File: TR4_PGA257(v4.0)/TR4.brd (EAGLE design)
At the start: 204 x 172 mm, 159 parts, among them IC1 SN74AVC4T774PWR, IC2 W25Q256JVFIQ, IC3 SN74AVC4T774PWR, IC4 SN74AVC4T774PWR, IC6 CP2102-GMR, IC7 LM1117MP-1.8_NOPB, IC8 LM1117MP-1.8_NOPB, IC9 LM1117MP-1.8_NOPB, J1 U-F-M5DD-Y-L, J3 TF-15X15, J4 2985-6004, J5 2985-6004, Q1 FMMT497TA, Q10 BSH103,235, Q11 BSH103,235, Q12 BSH103,235, Q13 BSH103,235, Q2 FMMT497TA, Q3 BSH103,235, Q4 BSH103,235, Q5 BSH103,235, Q6 BSH103,235, Q7 BSH103,235, Q8 BSH103,235, Q9 BSH103,235

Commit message: Add pull resistor for mosfet
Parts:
- added R61, R62, R63, R64, R65, R66, R67, R68, R69, R70, R71: 10k, SparkFun-Resistors:0603
- moved JP10 2.50 mm to (-75.5, 9.00)
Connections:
- net GND: now also R61.1, R62.1, R63.1, R64.1, R65.1, R66.1, R67.1, R68.1, R69.1, R70.1, R71.1
- net LED_0: now also R64.2
- net LED_1: now also R65.2
- net LED_2: now also R66.2
- net LED_3: now also R67.2
- net LED_4: now also R68.2
- net LED_5: now also R69.2
- net LED_6: now also R70.2
- net LED_7: now also R71.2
- net VDD_1.8_1: now also R63.2
- net VDD_1.8_2: now also R61.2
- net VDD_1.8_3: now also R62.2
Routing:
- net GND: track 1342.1 -> 1388.4 mm
- net LED_4: track 5.75 -> 9.13 mm
- net VDD_1.8_2: track 19.3 -> 22.6 mm
- net LED_3: track 6.12 -> 9.01 mm
- net LED_5: track 6.35 -> 9.22 mm
- net LED_6: track 6.96 -> 9.83 mm
- net LED_7: track 7.56 -> 10.4 mm
- net LED_1: track 7.33 -> 9.83 mm
- net LED_2: track 6.72 -> 9.22 mm
- net LED_0: track 7.93 -> 10.4 mm
- net GPIO_OUT[1]: track 109.0 -> 107.9 mm
- net GPIO_OUT[7]: track 112.1 -> 111.0 mm
- net GPIO_OUT[6]: track 108.1 -> 107.1 mm
- net GPIO_OUT[5]: track 111.0 -> 110.0 mm
- net GPIO_OUT[4]: track 107.1 -> 106.1 mm
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
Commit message: Update signal name and connect pin 59 and 60
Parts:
- removed C1, C10, C11, C6: 0.1uF, SparkFun-Capacitors:0603
- removed C12: 4.7uF, SparkFun-Capacitors:0603
- removed C9: 1.0uF, SparkFun-Capacitors:0603
- removed CHILDCLOCK, CLOCK: (no value), pinhead:2X02
- removed D1, D2, D3: (no value), SparkFun-LED:LED-0603
- removed IC2: W25Q256JVFIQ, SamacSys_Parts:SOIC127P1032X264-16N
- removed IC6: CP2102-GMR, SamacSys_Parts:QFN50P500X500X100-29N
- removed J1: U-F-M5DD-Y-L, SamacSys_Parts:UFM5DDYL
- removed J2: (no value), SparkFun-Connectors:1X07
- removed J3: TF-15X15, SamacSys_Parts:TF15X15
- removed JP7: PINHD-2X2, Connector:2X02
- removed Q1, Q2: FMMT497TA, SamacSys_Parts:SOT95P237X112-3N
- removed R11, R12, R13: 10k, SparkFun-Resistors:0603
- removed R14, R15, R16, R18, R19, R20, R21: 33, SparkFun-Resistors:0603
- removed R34, R35, R36, R40, R41, R43, R44: 4.7k, SparkFun-Resistors:0603
- removed R37, R38, R39: 330, SparkFun-Resistors:0603
- removed R42, R45: 47k, SparkFun-Resistors:0603
- removed R7, R8: 20k, SparkFun-Resistors:0603
- added FLASH, SD_CARD: PINHD-2X6, Connector:2X06
- added USB-UART: PINHD-2X4, Connector:2X04
- C14, C16, C18: value 10uF -> 100uF
- IC7, IC8, IC9: value LM1117MP-1.8_NOPB -> LM1117IMPX-ADJ/NOPB
- R1: value 200 -> 15k
- R2, R4, R6: value 20k -> 6.8k
- R3, R5: value 20k -> 15k
- moved R1 169.5 mm to (88.5, 50.0), turned to 270 degrees
- moved R2 156.2 mm to (86.5, 50.0), turned to 90 degrees
- moved R3 149.1 mm to (76.0, 50.0), turned to 270 degrees
- moved R6 149.0 mm to (61.5, 50.0)
- moved R4 146.8 mm to (74.0, 50.0), turned to 270 degrees
- moved R5 140.4 mm to (64.0, 50.0), turned to 270 degrees
- moved C4 9.62 mm to (83.0, -5.00)
- moved C5 9.62 mm to (83.0, -7.00)
- moved IC3 9.62 mm to (89.0, -10.0)
- moved R10 9.62 mm to (94.0, -7.00)
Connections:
- net VDD_CORE renamed VDD_CHIP
- net VDD_IO_CORE renamed VDD_CHIP_IO
- removed net CD1: R1.2, R8.1
- removed net D+: IC6.4, J1.3
- removed net D-: IC6.5, J1.2
- removed net DAT1: J3.8
- removed net DAT2: J3.1, R7.1
- removed net FLASH_HOLD: IC2.1, R12.1, R18.1
- removed net FLASH_RESET: IC2.3, R13.1, R16.1
- removed net FLASH_WP: IC2.9, R11.1, R21.1
- removed net N$1: J2.4, R14.2
- removed net N$11: J2.7, R21.2
- removed net N$2: J2.5, R19.2
- removed net N$25: IC6.9, R34.2
- removed net N$27: IC6.11, R35.2
- removed net N$29: IC6.12, R36.2
- removed net N$3: J3.9, R1.1
- removed net N$30: JP7.2, Q1.3, R40.1
- removed net N$31: Q1.1, R41.1
- removed net N$32: D1.A, R37.1
- removed net N$33: D2.A, R38.1
- removed net N$34: D3.A, R39.1
- removed net N$35: JP7.4, Q2.2, R44.2
- removed net N$36: R43.1, R44.1
- removed net N$37: Q2.1, R43.2
- removed net N$5: J2.3, R15.2
- removed net N$6: J2.6, R20.2
- removed net N$7: J2.1, R18.2
- removed net N$8: J2.2, R16.2
- removed net RXD: D3.C, IC6.25, Q2.3, R45.2
- removed net SMA_ICHILD: CHILDCLOCK.1, J5.5
- removed net SMA_ICLK: CLOCK.1, J4.5
- removed net TXD: D2.C, IC6.26, Q1.2, R42.1
- removed net VDD_5V: C10.1, C9.1, IC6.7, IC6.8, J1.1, R34.1, R35.1, R37.2
- removed net VDD_CP2102: C11.1, C12.1, IC6.6, R38.2, R39.2, R42.2, R45.1
- removed net VDD_IO: C3.1, C5.1, C8.1, IC1.1, IC1.16, IC1.2, IC1.7, IC3.1, IC3.16, IC3.2, IC3.8, IC4.16, IC4.8, JP8.2, R26.2, R27.2, R28.2, R29.2, R30.2, R31.2, R32.2, R33.2, R40.2, R41.2, R58.2, R59.2, R60.2
- new net VDD_1V8: C3.1, C5.1, C8.1, IC1.1, IC1.16, IC1.2, IC1.7, IC3.1, IC3.16, IC3.7, IC3.8, IC4.16, IC4.8, JP8.2, R26.2, R27.2, R28.2, R29.2, R30.2, R31.2, R32.2, R33.2, R58.2, R59.2, R60.2, USB-UART.5
- net B1: now also SD_CARD.12; no longer J3.2, R2.1
- net B2: now also SD_CARD.10; no longer J3.3, R3.1
- net B3: now also SD_CARD.6; no longer J3.5, R4.1
- net B4: now also SD_CARD.8; no longer J3.7, R5.1
- net CHILDCLOCK: now also J5.5; no longer CHILDCLOCK.2, CHILDCLOCK.4
- net CHILDCLOCK_GPIO: no longer CHILDCLOCK.3
- net CLOCK_GPIO: no longer CLOCK.3
- net CS: now also IC3.3, JP2.2; no longer IC3.6, JP2.8
- net DAT0: no longer R6.1
- net FLASH_CS: now also FLASH.12, IC3.14; no longer IC2.8, IC3.11, R15.1
- net FLASH_MISO: now also FLASH.8, IC3.13; no longer IC2.7, IC3.12, R14.1
- net FLASH_MOSI: now also FLASH.10, IC3.12; no longer IC2.15, IC3.13, R19.1
- net FLASH_SCK: now also FLASH.6, IC3.11; no longer IC2.16, IC3.14, R20.1
- net GND: now also FLASH.3, FLASH.4, IC3.2, R1.1, R2.1, R2.2, R3.1, R4.1, R4.2, R5.1, R6.1, R6.2, SD_CARD.3, SD_CARD.4, USB-UART.1; no longer C1.2, C10.2, C11.2, C12.2, C6.2, C9.2, D1.C, IC2.10, IC3.7, IC6.3, J1.10, J1.5, J1.7, J1.8, J1.9, J3.6, J3.MP1, J3.MP2, J3.MP3, J3.MP4, R36.1
- net MISO: now also IC3.4, JP2.4; no longer IC3.5, JP2.6
- net MOSI: now also IC3.5, JP2.6; no longer IC3.4, JP2.4
- net QSPI_CS: now also JP2.1; no longer JP2.7
- net QSPI_MISO: now also JP2.3; no longer JP2.5
- net QSPI_MOSI: now also JP2.5; no longer JP2.3
- net QSPI_SCK: now also JP2.7; no longer JP2.1
- net SCK: now also IC3.6, JP2.8; no longer IC3.3, JP2.2
- net SYS_CLK: now also J4.5; no longer CLOCK.2, CLOCK.4
- net TLPORT_A_BITS_PARAM[0]: now also SOCKET_2.28
- net UART_RXD: now also USB-UART.3; no longer JP7.1
- net UART_TXD: now also USB-UART.7; no longer JP7.3
- net VDD_1.8_1: now also R1.2
- net VDD_1.8_2: now also R3.2
- net VDD_1.8_3: now also R5.2
- net VDD_3V3: now also FLASH.1, FLASH.2, SD_CARD.1, SD_CARD.2; no longer C1.1, C6.1, IC2.2, J3.4, R11.2, R12.2, R13.2, R2.2, R3.2, R4.2, R5.2, R6.2, R7.2, R8.2
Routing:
- net VDD_1V8: track 0.00 -> 658.1 mm, vias 0 -> 17
- net VDD_IO: track 648.5 -> 0.00 mm, vias 17 -> 0
- net GND: track 1388.4 -> 1239.0 mm, vias 261 -> 256
- net CLOCK_GPIO: track 45.6 -> 0.00 mm
- net FLASH_HOLD: track 39.8 -> 0.00 mm, vias 2 -> 0
- net UART_RXD: track 15.7 -> 54.8 mm, vias 0 -> 1
- net VDD_3V3: track 726.5 -> 687.8 mm, vias 0 -> 3
- net FLASH_RESET: track 35.6 -> 0.00 mm, vias 2 -> 0
- net UART_TXD: track 18.3 -> 52.5 mm, vias 0 -> 1
- net VDD_5V: track 34.1 -> 0.00 mm
- net CHILDCLOCK_GPIO: track 33.6 -> 0.00 mm
- net VDD_CP2102: track 28.0 -> 0.00 mm
- net FLASH_WP: track 26.0 -> 0.00 mm, vias 2 -> 0
- net D-: track 24.9 -> 0.00 mm, vias 2 -> 0
- net D+: track 24.0 -> 0.00 mm, vias 2 -> 0
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- added copper zone on layer 1, net VDD_1V8
- added copper zone on layer 16, net VDD_1V8
- added copper zone on layer 16, net VDD_3V3
- removed copper zone on layer 1, net CHILDCLOCK_GPIO
- removed copper zone on layer 1, net CLOCK_GPIO
- removed copper zone on layer 1, net SMA_ICHILD
- removed copper zone on layer 1, net SMA_ICLK
- removed copper zone on layer 1, net VDD_5V
- removed copper zone on layer 1, net VDD_IO
- removed copper zone on layer 16, net VDD_IO
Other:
- board text added: "1.8V CHIP"
- board text added: "1.8V CHIP IO"
- board text added: "CHILD_CLOCK"
- board text added: "CLK"
- board text added: "CMD"
- board text added: "DAT_0"
- board text added: "DAT_3"
- board text added: "FLASH_CS"
- board text added: "FLASH_MISO"
- board text added: "FLASH_MOSI"
- board text added: "FLASH_SCK"
- board text added: "SD card"
- board text added: "SYSTEM_CLOCK"
- board text removed: "1.8V CORE"
- board text removed: "1.8V IO CORE"
- board text removed: "FLASH_WP FLASH_SCK FLASH_MOSI FLASH_MISO FLASH_CS FLASH_RESET FLASH_HOLD"
- board text removed: "RX"
- board text removed: "SMA"
- board text removed: "SPI"
- board text removed: "TX"
- board text removed: "USB Power (5V)"

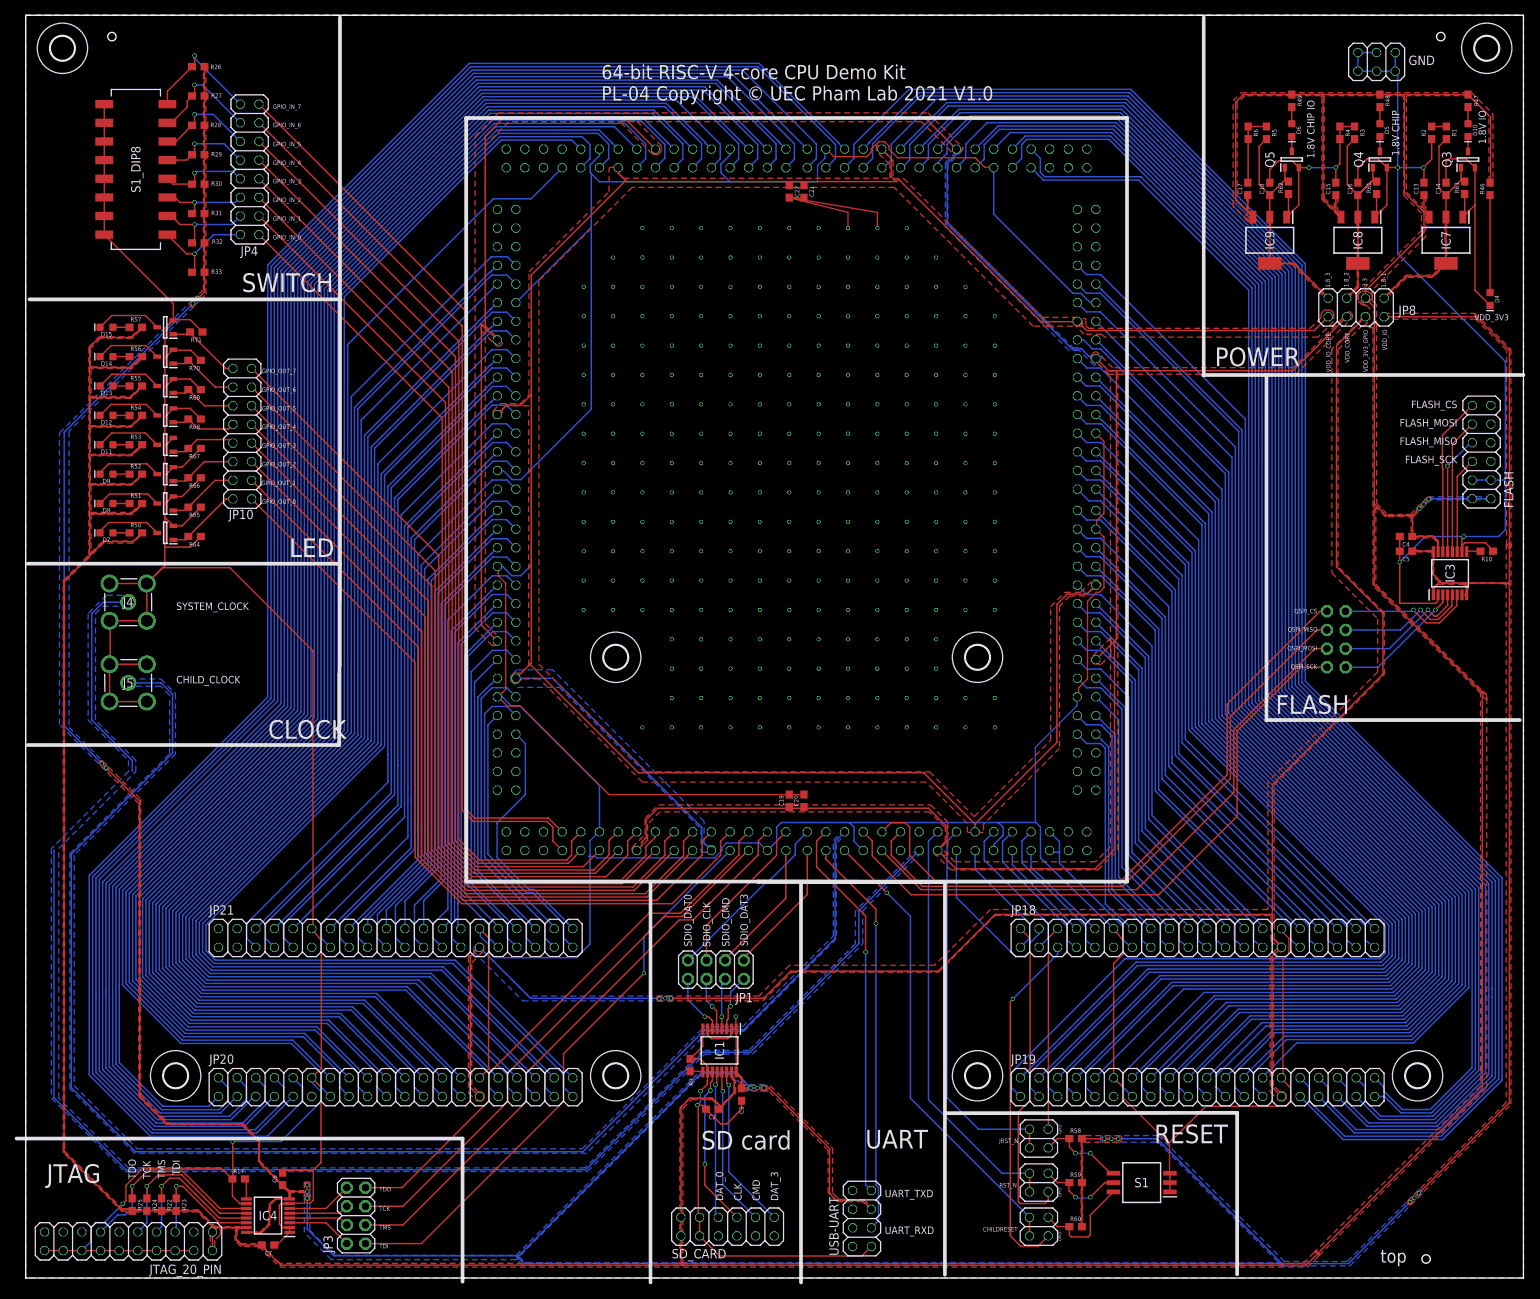
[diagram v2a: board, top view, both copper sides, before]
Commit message: put header for param[0] signal
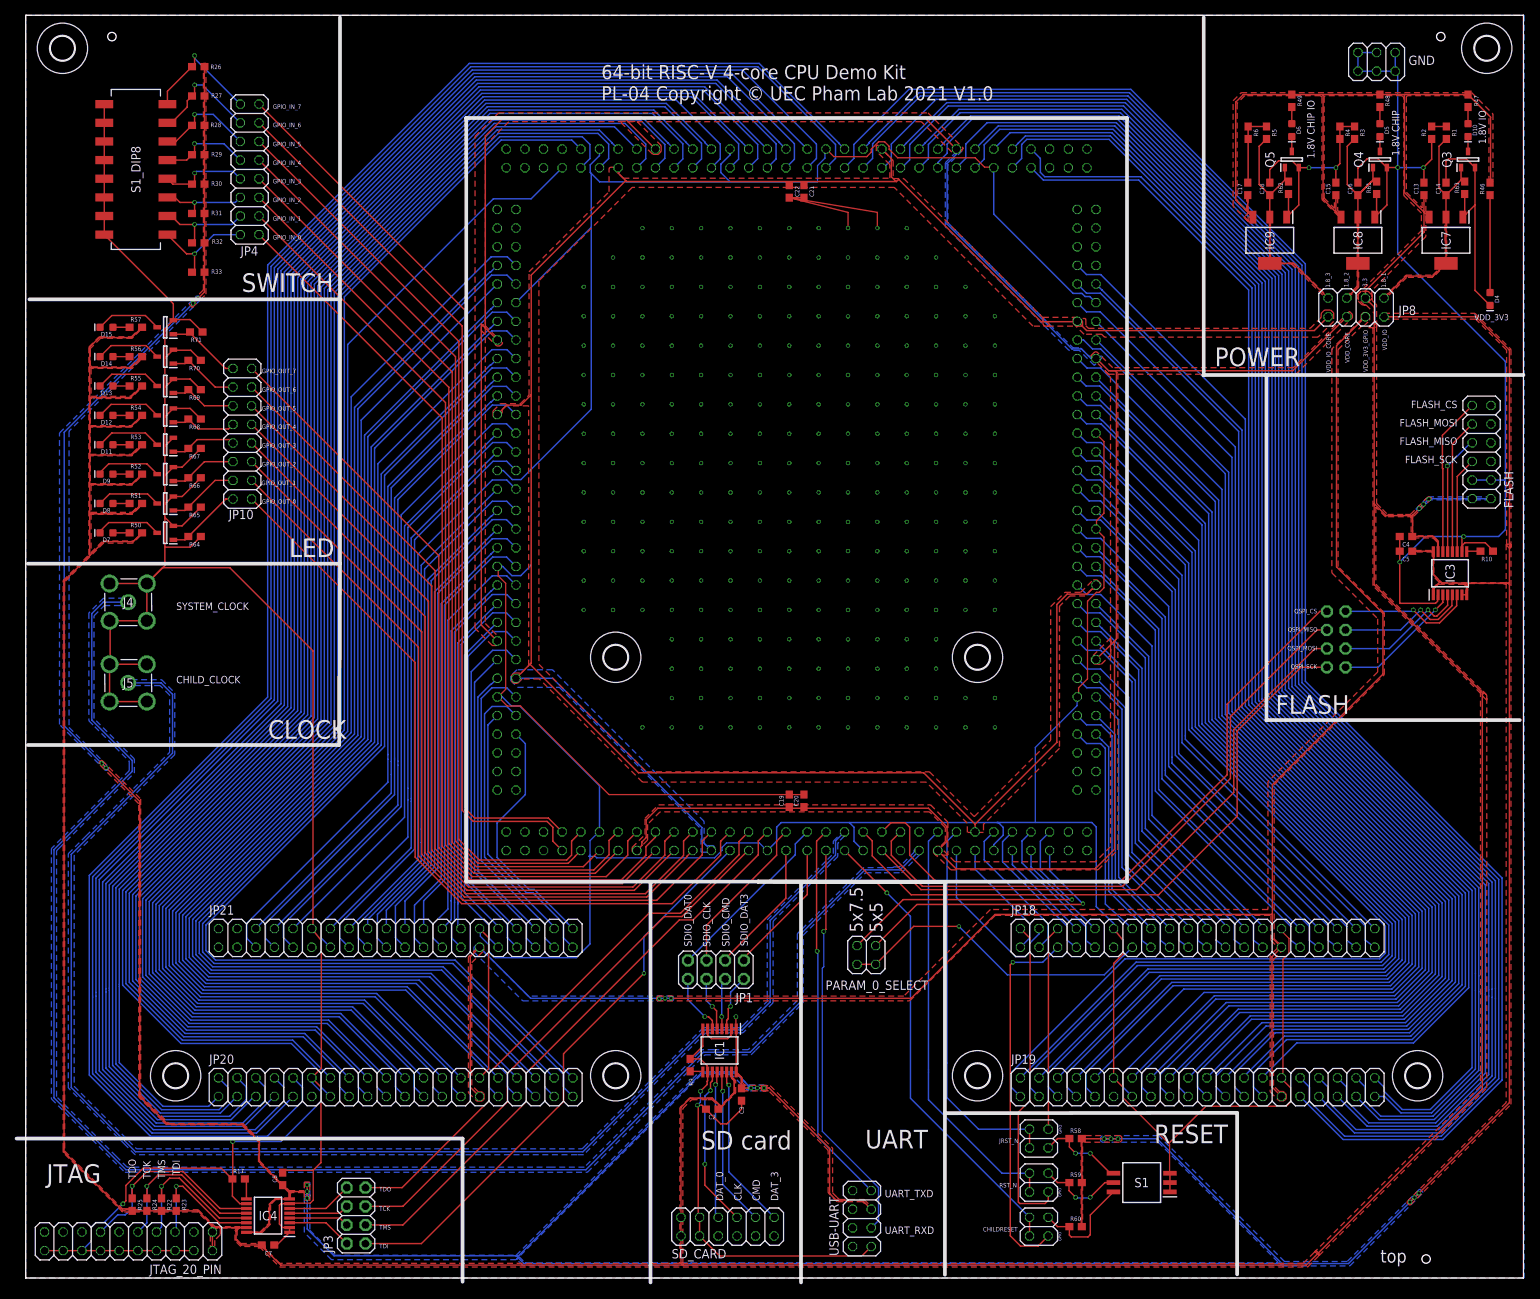
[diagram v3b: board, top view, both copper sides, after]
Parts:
- added PARAM_0_SELECT: PINHD-2X2, Connector:2X02
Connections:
- new net PARAM[0]_5X5: PARAM_0_SELECT.1, SOCKET_2.28
- new net PARAM[0]_5X7.5: PARAM_0_SELECT.3, SOCKET_2.27
- net TLPORT_A_BITS_PARAM[0]: now also PARAM_0_SELECT.2, PARAM_0_SELECT.4; no longer SOCKET_2.27, SOCKET_2.28
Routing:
- net PARAM[0]_5X7.5: track 0.00 -> 43.6 mm, vias 0 -> 1
- net PARAM[0]_5X5: track 0.00 -> 39.7 mm, vias 0 -> 1
- net TLPORT_A_BITS_PARAM[0]: track 21.9 -> 43.9 mm, vias 0 -> 1
- net SYS_CLK: track 205.7 -> 223.6 mm
- net GND: track 1239.0 -> 1243.9 mm
- net CHILDRESET_GPIO: track 48.3 -> 50.7 mm
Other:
- board text added: "5x5"
- board text added: "5x7.5"

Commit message: update for order
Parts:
- removed C7, C8: 0.1uF, SparkFun-Capacitors:0603
- removed IC4: SN74AVC4T774PWR, SamacSys_Parts:SOP65P640X120-16N
- removed R10, R17: 10k, SparkFun-Resistors:0603
- added C1, C6: 0.1uF, SparkFun-Capacitors:0603
- added IC2: SN74AVC4T774RSVR, SamacSys_Parts:QFN40P180X260X55-16N
- added R7, R8: 10k, SparkFun-Resistors:0603
- IC1, IC3: value SN74AVC4T774PWR -> SN74AVC4T774RSVR; device SamacSys_Parts:SOP65P640X120-16N -> SamacSys_Parts:QFN40P180X260X55-16N
- moved C4 186.8 mm to (-77.5, -100.5), turned to 270 degrees
- moved IC3 185.4 mm to (-74.5, -97.5), turned to 180 degrees
- moved C5 178.8 mm to (-73.5, -93.5), turned to 90 degrees
- moved C2 118.1 mm to (80.5, -9.00), turned to 90 degrees
- moved C3 117.8 mm to (88.0, -12.0), turned to 0 degrees
- moved IC1 114.5 mm to (84.3, -10.8), turned to 90 degrees
- moved R9 63.2 mm to (-75.5, -93.5)
- flipped JP2 to the top, turned to 270 degrees
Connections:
- removed net CLK: IC1.5, JP1.6
- removed net CMD: IC1.4, JP1.4
- removed net CS: IC3.3, JP2.2
- removed net DAT0: IC1.6, JP1.8
- removed net DAT3: IC1.3, JP1.2
- removed net MISO: IC3.4, JP2.4
- removed net MOSI: IC3.5, JP2.6
- removed net N$16: IC4.9, R17.2
- removed net SCK: IC3.6, JP2.8
- new net N$1: IC2.7, R7.2
- new net N$11: IC1.1, JP2.2
- new net N$2: IC2.1, JP1.2
- new net N$25: IC3.7, R9.2
- new net N$3: IC2.2, JP1.4
- new net N$5: IC2.3, JP1.6
- new net N$6: IC2.4, JP1.8
- new net N$7: IC1.7, R8.2
- new net N$8: IC1.4, JP2.8
- net B1: now also IC2.12; no longer IC1.14
- net B2: now also IC2.11; no longer IC1.13
- net B3: now also IC2.10; no longer IC1.12
- net B4: now also IC2.9; no longer IC1.11
- net FLASH_CS: now also IC1.12; no longer IC3.14
- net FLASH_MISO: now also IC1.11; no longer IC3.13
- net FLASH_MOSI: now also IC1.10; no longer IC3.12
- net FLASH_SCK: now also IC1.9; no longer IC3.11
- net GND: now also C1.2, C6.2, IC1.16, IC2.6, IC2.8, IC3.15, IC3.16, IC3.5, IC3.8, R7.1, R8.1; no longer C7.2, C8.2, IC1.10, IC3.10, IC3.2, IC4.1, IC4.10, IC4.2, IC4.7, R10.1, R17.1
- net N$10: now also IC1.2, JP2.4; no longer IC3.9, R10.2
- net N$12: now also IC3.1; no longer IC4.3
- net N$13: now also IC3.2; no longer IC4.4
- net N$14: now also IC3.3; no longer IC4.5
- net N$15: now also IC3.4; no longer IC4.6
- net N$9: now also IC1.3, JP2.6; no longer IC1.9, R9.2
- net TCK: now also IC3.10; no longer IC4.12
- net TDI: now also IC3.12; no longer IC4.14
- net TDO: now also IC3.9; no longer IC4.11
- net TMS: now also IC3.11; no longer IC4.13
- net VDD_1V8: now also C6.1, IC1.14, IC1.15, IC1.5, IC1.6, IC2.14, IC2.15, IC2.16, IC2.5, IC3.14, IC3.6; no longer C8.1, IC1.1, IC1.16, IC1.2, IC1.7, IC3.1, IC3.16, IC3.7, IC3.8, IC4.16, IC4.8
- net VDD_3V3: now also C1.1, IC1.13, IC2.13, IC3.13; no longer C7.1, IC1.15, IC3.15, IC4.15
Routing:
- net VDD_1V8: track 658.1 -> 680.9 mm
- net MISO: track 18.5 -> 0.00 mm, vias 1 -> 0
- net MOSI: track 18.5 -> 0.00 mm, vias 1 -> 0
- net SCK: track 18.4 -> 0.00 mm, vias 1 -> 0
- net CS: track 18.0 -> 0.00 mm, vias 1 -> 0
- net N$8: track 0.00 -> 16.7 mm, vias 0 -> 1
- net GND: track 1243.9 -> 1259.1 mm, vias 256 -> 257
- net N$9: track 1.76 -> 14.7 mm, vias 0 -> 1
- net N$11: track 0.00 -> 11.0 mm, vias 0 -> 1
- net N$10: track 1.90 -> 12.6 mm, vias 0 -> 1
- net N$6: track 0.00 -> 8.62 mm
- net DAT0: track 8.47 -> 0.00 mm, vias 1 -> 0
- net N$2: track 0.00 -> 7.80 mm
- net DAT3: track 7.76 -> 0.00 mm, vias 1 -> 0
- net N$5: track 0.00 -> 7.74 mm
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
